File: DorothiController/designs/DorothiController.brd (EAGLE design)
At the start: 76.2 x 30.5 mm, 28 parts

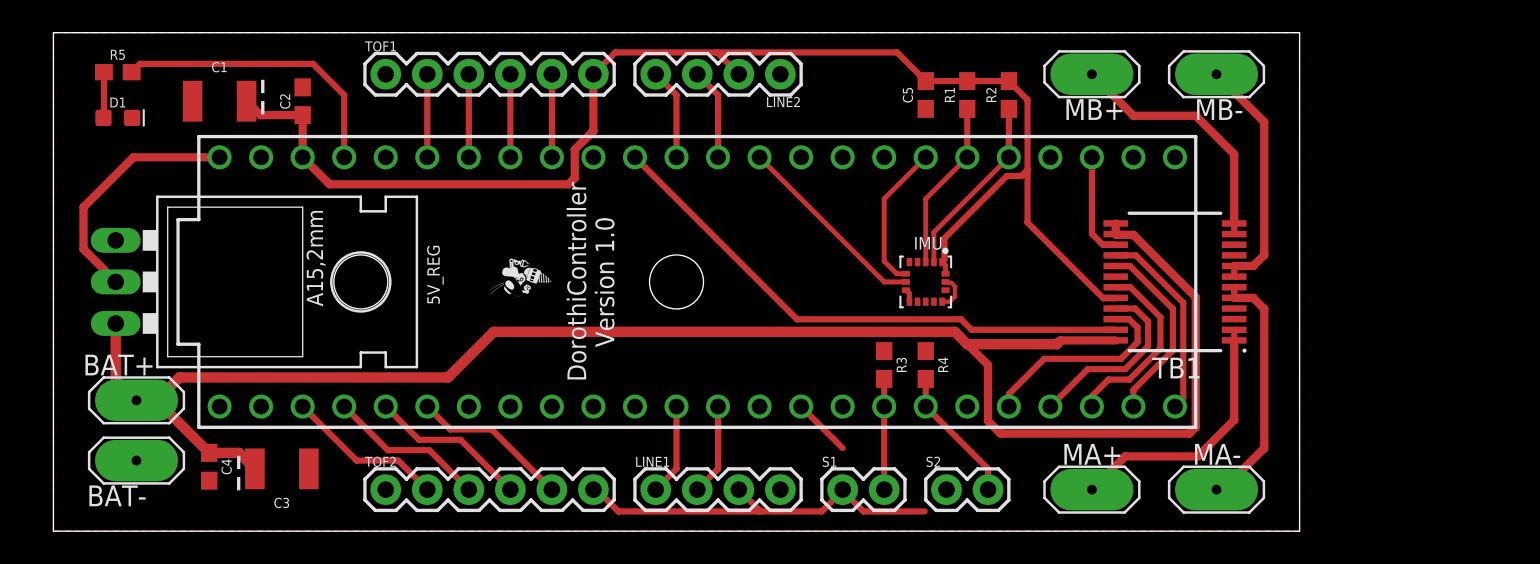
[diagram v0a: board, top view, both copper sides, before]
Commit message: new 2 layer board with encoders
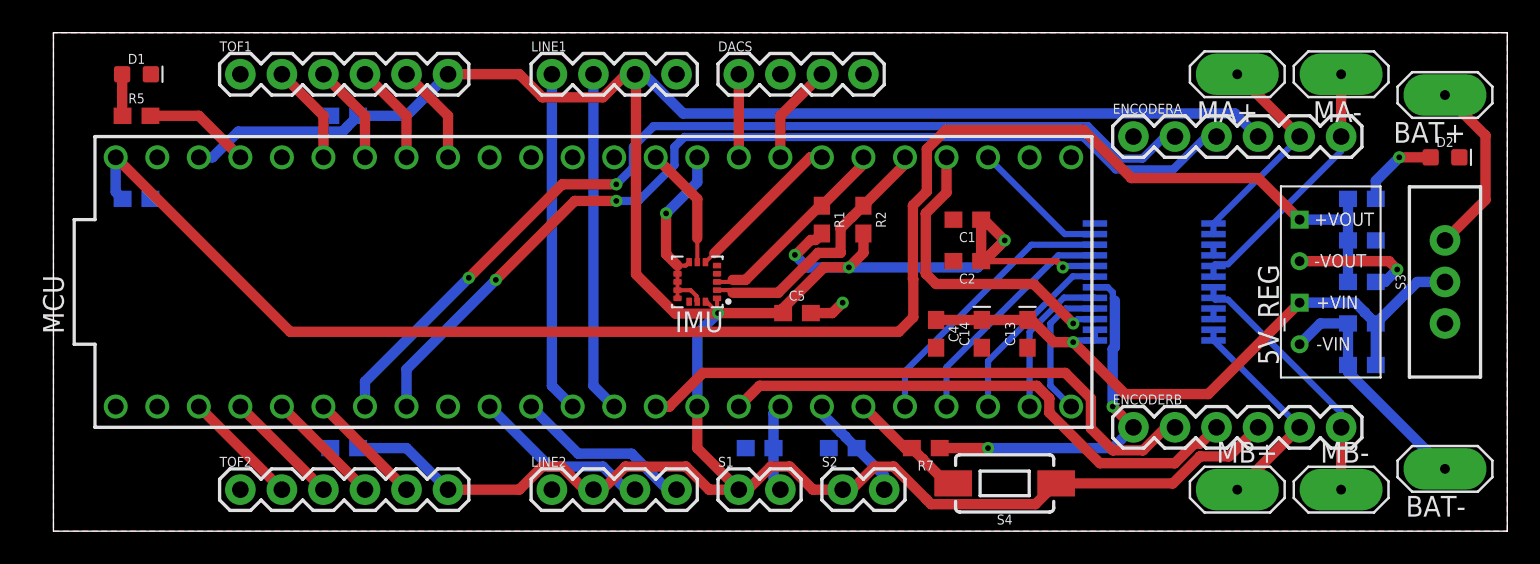
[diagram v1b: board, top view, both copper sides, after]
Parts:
- removed U$1: TEENSY_3.6_DIL, Teensy_3_and_LC_Series_Boards_v1.4:TEENSY_3.6_DIL
- removed U$2: ROBOBUZZ0.2X, RoboJackets-Aesthetics:ROBOBUZZ_0.2X
- added C10: 10uF, SparkFun-Capacitors:0603
- added C11, C6: 1.0uF, SparkFun-Capacitors:0603
- added C13, C14: 10uF, SparkFun-Capacitors:0603-POLAR
- added C7, C8, C9: 0.1uF, SparkFun-Capacitors:0603
- added D2: (no value), SparkFun-LED:LED-0603
- added DACS: (no value), SparkFun-Connectors:1X04
- added ENCODERA, ENCODERB: (no value), SparkFun-Connectors:1X06
- added MCU: TEENSY_3.6_DIL, Teensy_3_and_LC_Series_Boards_v1.4:TEENSY_3.6_DIL
- added R6: 10k, SparkFun-Resistors:0603
- added R7: 1k, SparkFun-Resistors:0603
- added S3: ONOFF, SparkFun-Switches:SWITCH_SPDT_PTH_11.6X4.0MM
- added S4: START, SparkFun-Switches:TACTILE_SWITCH_SMD_6.0X3.5MM
- 5V_REG: value (none) -> CRE1S1205SC; device v-reg:TO220L1 -> CRE1S1205SC:CRE1S1205SC
- C1: device SparkFun-Capacitors:EIA3528 -> SparkFun-Capacitors:0603
- C3: value 10uF -> 0.1uF; device SparkFun-Capacitors:EIA3528 -> SparkFun-Capacitors:0603
- moved BAT+ 82.2 mm to (85.1, 26.7)
- moved BAT- 80.0 mm to (85.1, 3.81)
- moved 5V_REG 68.6 mm to (76.2, 15.2), turned to 90 degrees
- moved C1 46.3 mm to (55.9, 19.1), turned to 180 degrees
- moved C4 45.2 mm to (54.0, 12.1)
- moved C2 41.8 mm to (55.9, 16.5), turned to 180 degrees
- moved LINE2 29.0 mm to (30.5, 2.54), turned to 0 degrees
- moved MA+ 26.9 mm to (72.4, 27.9)
- moved MB+ 26.9 mm to (72.4, 2.54), turned to 0 degrees
- moved MA- 26.5 mm to (78.7, 27.9)
- moved MB- 26.5 mm to (78.7, 2.54), turned to 0 degrees
- moved LINE1 26.2 mm to (30.5, 27.9)
- moved C3 18.8 mm to (5.08, 20.3), flipped to the bottom
- moved C5 15.5 mm to (45.5, 13.3), turned to 0 degrees
- moved IMU 14.0 mm to (39.4, 15.2), turned to 180 degrees
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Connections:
- new net +VIN: BAT+.P$1, S3.1
- new net -VIN: 5V_REG.-VIN, BAT-.P$1, C10.2, C6.2
- new net DAC1: DACS.1, MCU.A22
- new net DAC2: DACS.3, MCU.A21
- new net ENCA_OUTA: ENCODERA.3, MCU.6
- new net ENCA_OUTB: ENCODERA.2, MCU.5
- new net ENCB_OUTA: ENCODERB.3, MCU.24
- new net ENCB_OUTB: ENCODERB.2, MCU.12
- new net N$7: D2.A, R6.1
- new net START: MCU.27, R7.2, S4.2
- new net VM1: TB1.24
- net +12V: now also 5V_REG.+VIN, C10.1, C13.+, C14.+, C6.1, S3.2; no longer 5V_REG.3, BAT+.P$1, C3.A, TB1.24
- net +3V3: now also C1.1, C8.1, C9.1, ENCODERA.4, ENCODERB.4, MCU.3.3V, MCU.3.3V3, S4.1; no longer C1.A, U$1.3.3V, U$1.3.3V3
- net 5V_OUT: now also 5V_REG.+VOUT, C11.1, C3.1, C7.1, MCU.VIN, R6.2; no longer 5V_REG.2, U$1.VIN
- net BTN1: now also MCU.25; no longer U$1.25
- net BTN2: now also MCU.26; no longer U$1.26
- net GND: now also 5V_REG.-VOUT, C1.2, C11.2, C13.-, C14.-, C3.2, C7.2, C8.2, C9.2, D2.C, DACS.2, DACS.4, ENCODERA.1, ENCODERB.1, MCU.AGND, MCU.GND, MCU.GND1, R7.1; no longer 5V_REG.1, BAT-.P$1, C1.C, C3.C, U$1.AGND, U$1.GND, U$1.GND1
- net IMU_INT1: now also MCU.13; no longer U$1.13
- net IMU_INT2: now also MCU.39/A20; no longer U$1.39/A20
- net IMU_SCL: now also MCU.37/A18; no longer U$1.37/A18
- net IMU_SDA: now also MCU.38/A19; no longer U$1.38/A19
- net INDICATOR: now also MCU.23/A9; no longer U$1.23/A9
- net LINE1_RS1: now also MCU.10; no longer U$1.10
- net LINE1_RS2: now also MCU.11; no longer U$1.11
- net LINE2_RS1: now also MCU.8; no longer U$1.14/A0
- net LINE2_RS2: now also MCU.9; no longer U$1.15/A1
- net MA+: now also ENCODERA.5
- net MA-: now also ENCODERA.6
- net MB+: now also ENCODERB.5
- net MB-: now also ENCODERB.6
- net M_AIN1: now also MCU.29; no longer U$1.29
- net M_AIN2: now also MCU.28; no longer U$1.28
- net M_BIN1: now also MCU.31/A12; no longer U$1.31/A12
- net M_BIN2: now also MCU.32/A13; no longer U$1.32/A13
- net M_PWMA: now also MCU.35/A16; no longer U$1.16/A2
- net M_PWMB: now also MCU.36/A17; no longer U$1.35/A16
- net M_STBY: now also MCU.30; no longer U$1.30
- net TOF1_READY: now also MCU.20/A6; no longer U$1.20/A6
- net TOF1_SCL: now also MCU.19/A5; no longer U$1.19/A5
- net TOF1_SDA: now also MCU.18/A4; no longer U$1.18/A4
- net TOF1_SHDN: now also MCU.21/A7; no longer U$1.21/A7
- net TOF2_READY: now also MCU.2; no longer U$1.2
- net TOF2_SCL: now also MCU.3; no longer U$1.3
- net TOF2_SDA: now also MCU.4; no longer U$1.4
- net TOF2_SHDN: now also MCU.1; no longer U$1.1
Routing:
- net +3V3: track 112.1 -> 206.7 mm, vias 0 -> 5
- net 5V_OUT: track 15.0 -> 100.5 mm
- net +12V: track 108.5 -> 41.5 mm, vias 0 -> 1
- net ENCA_OUTA: track 0.00 -> 60.0 mm, vias 0 -> 2
- net ENCA_OUTB: track 0.00 -> 59.6 mm, vias 0 -> 2
- net GND: track 3.01 -> 46.0 mm, vias 0 -> 5
- net ENCB_OUTB: track 0.00 -> 36.2 mm
- net ENCB_OUTA: track 0.00 -> 33.1 mm
- net M_PWMA: track 33.8 -> 8.48 mm
- net LINE1_RS2: track 5.61 -> 20.8 mm
- net LINE1_RS1: track 5.61 -> 20.8 mm
- net -VIN: track 0.00 -> 14.8 mm
- net M_PWMB: track 6.41 -> 19.4 mm, vias 0 -> 1
- net INDICATOR: track 17.8 -> 6.55 mm
- net +VIN: track 0.00 -> 10.9 mm
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- added copper zone on layer 16, net GND
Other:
- board size 76.2 x 30.5 mm -> 88.9 x 30.5 mm
- board text removed: "DorothiController Version 1.0"
